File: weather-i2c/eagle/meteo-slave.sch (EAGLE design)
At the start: 41 parts, among them CON1 SPI, IC1 MCP1703CB, J2 RJ12RIGHTANGLE-I2C, J3 RJ12RIGHTANGLE-I2C, U1 ATMEGA328P_TQFP, X1 8MHz, X2 1503_09, X3 1503_09

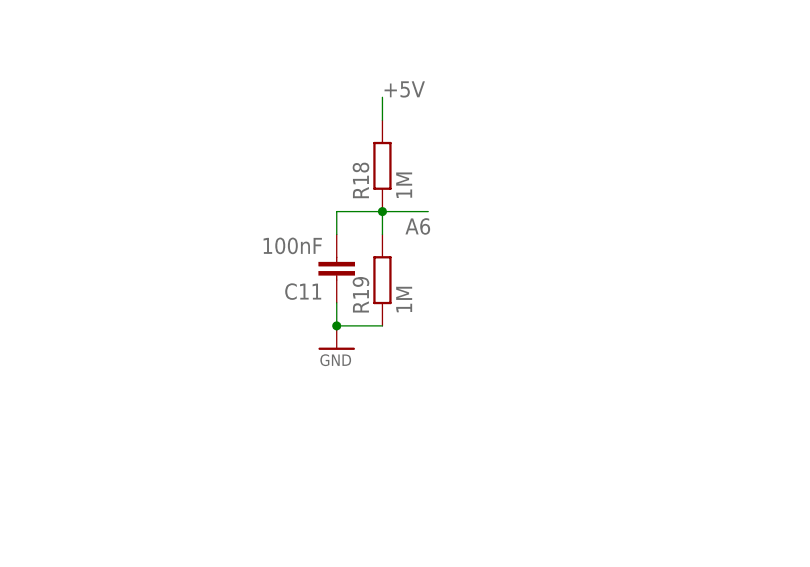
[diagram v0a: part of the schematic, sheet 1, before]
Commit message: weather-i2c: fix voltage check resistor value
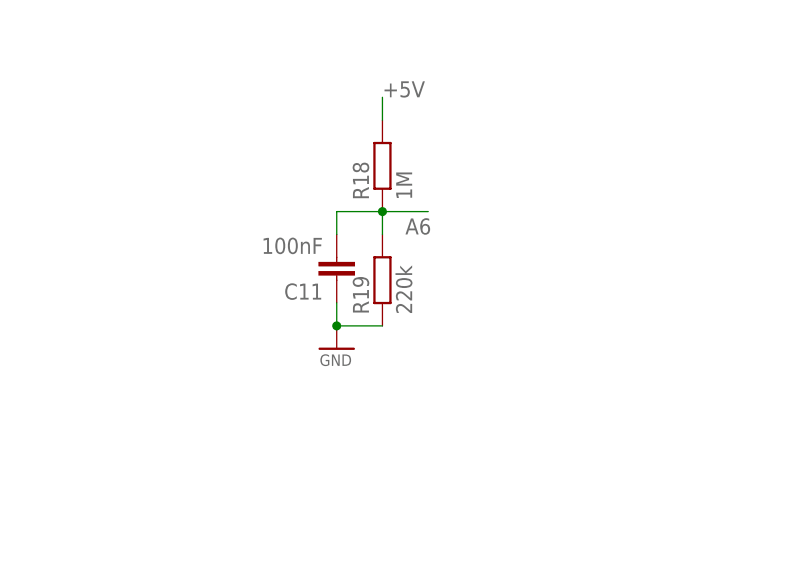
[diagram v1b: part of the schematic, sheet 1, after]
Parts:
- R19: value 1M -> 220k
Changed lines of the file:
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@@
 <?xml version="1.0" encoding="utf-8"?>
 <!DOCTYPE eagle SYSTEM "eagle.dtd">
-<eagle version="9.0.0">
+<eagle version="9.1.0">
 <drawing>
 <settings>
@@
 <attribute name="LCSC" value="C17514"/>
 </part>
-<part name="R19" library="rcl" deviceset="R-EU_" device="R0805" value="1M">
+<part name="R19" library="rcl" deviceset="R-EU_" device="R0805" value="220k">
 <attribute name="ELECROW" value="C17514"/>
 <attribute name="LCSC" value="C17514"/>
